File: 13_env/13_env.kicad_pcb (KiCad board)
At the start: 2 copper layers, 30 x 100 mm, 51 parts, among them J1 gate in 1, J3 Eurorack, J5 env out 1, J6 End of Cycle Out, Q1 BC848, Q2 BC858, Q3 BC848, Q4 BC858, SW1 Manual Gate, SW2 Normal/Inverted, SW4 Gate/Loop, U1 TL074, U2 TL072

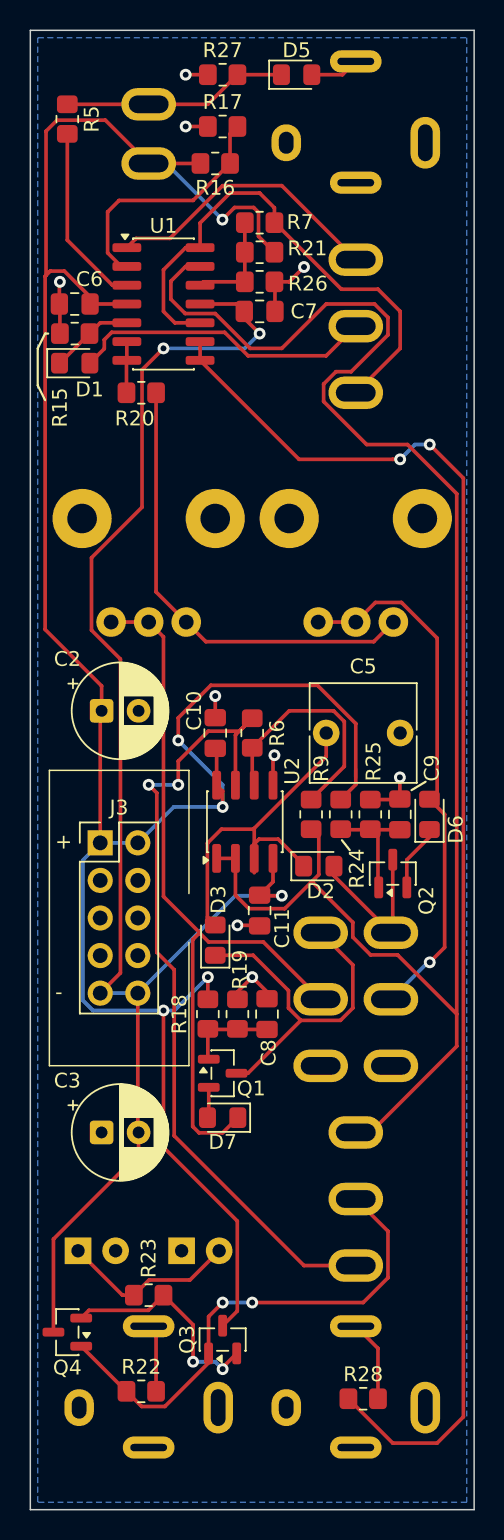
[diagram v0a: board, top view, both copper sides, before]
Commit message: added diodes
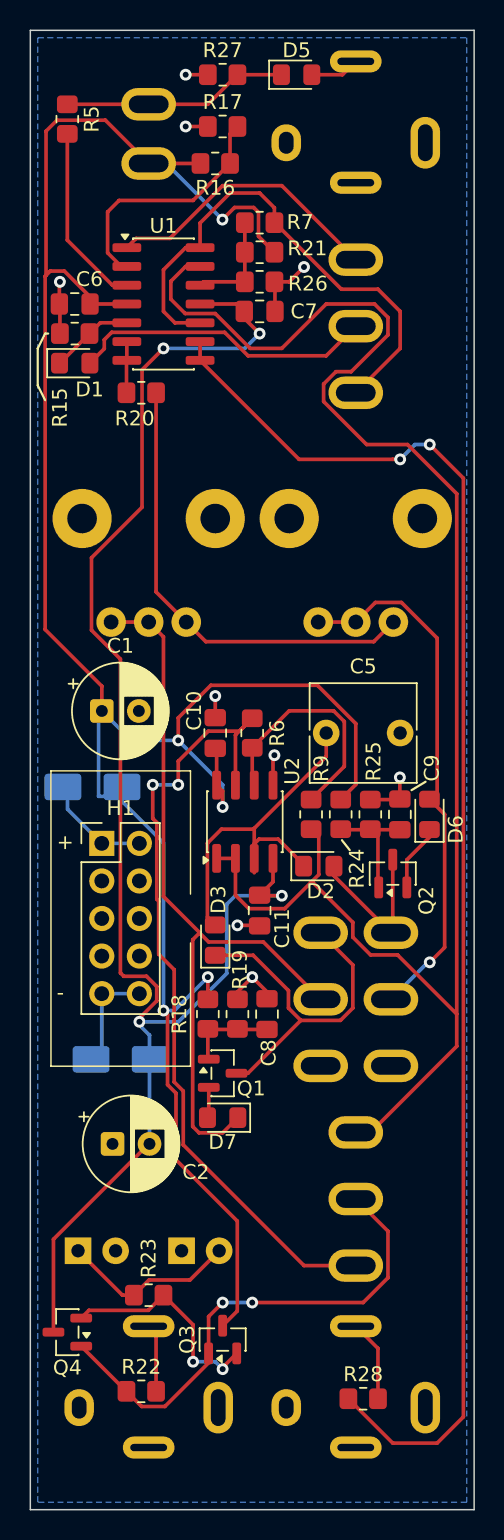
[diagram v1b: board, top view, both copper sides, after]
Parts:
- removed C3: 50uF, Capacitor_THT:CP_Radial_D6.3mm_P2.50mm
- removed J3: Eurorack, cynthia:Eurorack Header
- added C1: 22uF, Capacitor_THT:CP_Radial_D6.3mm_P2.50mm, F.Cu at (-0.17, 50.5)
- added D11: SS14, Diode_SMD:D_SMA, B.Cu at (1.10, 74.1)
- added D12: SS14, Diode_SMD:D_SMA, B.Cu at (-0.80, 55.6)
- added H1: Eurorack 10 pin header, cynthia:Eurorack Header, F.Cu at (-0.17, 59.5)
- C2: value 50uF -> 22uF
- moved C2 29.3 mm to (0.56, 79.8)
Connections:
- C2 pad 1: +12V -> GND
- C2 pad 2: GND -> -12V
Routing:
- net Net-(D11-K): track 0.00 -> 7.28 mm
- net +12V: track 168.9 -> 161.7 mm
- net Net-(D12-A): track 0.00 -> 6.68 mm
- net -12V: track 103.7 -> 107.1 mm, vias 3 -> 4

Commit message: updated 13 pcb
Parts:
- C1, C2, H1, Q1, Q2, Q3, Q4, U1, U2: moved to B.Cu
- C10, C11, C6, C7, C8, C9: footprint Capacitor_SMD:C_0805_2012Metric_Pad1.18x1.45mm_HandSolder -> cynthia:C SMD 0805; moved to B.Cu
- D1, D2, D3, D5, D6, D7: footprint Diode_SMD:D_0805_2012Metric_Pad1.15x1.40mm_HandSolder -> Diode_SMD:D_SOD-323_HandSoldering; moved to B.Cu
- D4, D8, J1, J5, J6, RV2, RV3, SW1, SW2, SW3, SW4: moved to F.Cu
- R15, R16, R17, R18, R19, R20, R21, R22, R23, R24, R25, R26, R27, R28, R5, R6, R7, R9: footprint Resistor_SMD:R_0805_2012Metric_Pad1.20x1.40mm_HandSolder -> cynthia:R SMD 0805; moved to B.Cu
- moved R28 85.0 mm to (17.0, 12.0), turned to 180 degrees
- moved J6 85.0 mm to (17.0, 12.0), turned to 0 degrees
- moved D11 36.7 mm to (-2.00, 37.5), turned to -90 degrees
- moved C2 32.7 mm to (4.18, 47.3), turned to 180 degrees
- moved R24 30.3 mm to (-2.50, 81.5), turned to -90 degrees
- moved R25 30.0 mm to (0.00, 81.5), turned to 90 degrees
- moved C9 29.7 mm to (2.50, 81.5), turned to -90 degrees
- moved D12 27.8 mm to (22.0, 39.8), turned to 90 degrees
- moved R5 27.4 mm to (23.0, 20.5), turned to 90 degrees
- moved D6 26.4 mm to (3.67, 76.5), turned to -90 degrees
- moved D8 26.0 mm to (21.5, 98.5), turned to 180 degrees
- moved H1 24.9 mm to (15.2, 39.9), turned to 90 degrees
- moved Q2 24.2 mm to (0.50, 76.5), turned to 0 degrees
- moved SW1 20.9 mm to (17.0, 27.0), turned to 0 degrees
- moved RV2 19.4 mm to (3.00, 51.0), turned to 0 degrees
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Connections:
- R20 pad 1: Net-(U1B--) -> Net-(U1D--)
- R21 pad 1: Net-(U1D-+) -> Net-(U1B-+)
- R26 pad 2: Net-(U1D-+) -> Net-(U1B-+)
- R7 pad 1: Net-(U1D-+) -> Net-(U1B-+)
- U1 pad 12: Net-(U1D-+) -> Net-(D1-K)
- U1 pad 13: Net-(SW2-A) -> Net-(U1D--)
- U1 pad 14: Net-(SW4-A) -> Net-(U1D--)
- U1 pad 5: Net-(D1-K) -> Net-(U1B-+)
- U1 pad 6: Net-(U1B--) -> Net-(SW2-A)
- U1 pad 7: Net-(U1B--) -> Net-(SW4-A)
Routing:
- net Net-(U1C--): track 96.4 -> 21.2 mm, vias 2 -> 0
- net Net-(D5-K): track 15.3 -> 57.5 mm
- net Net-(SW2-C): track 55.1 -> 21.9 mm, vias 2 -> 0
- net Net-(SW2-A): track 115.4 -> 88.8 mm, vias 0 -> 4
- net +12V: track 161.7 -> 140.4 mm, vias 5 -> 4
- net Net-(D1-A): track 20.7 -> 4.21 mm
- net Net-(U1B-+): track 0.00 -> 16.0 mm
- net Net-(Q3-B): track 34.1 -> 49.5 mm, vias 2 -> 0
- net Net-(D4-A): track 12.0 -> 27.1 mm
- net Net-(U1D--): track 0.00 -> 14.2 mm, vias 0 -> 2
- net Net-(R20-Pad2): track 31.4 -> 45.6 mm
- net -12V: track 107.1 -> 119.8 mm, vias 4 -> 3
- net Net-(D3-K): track 24.0 -> 12.3 mm
- net Net-(D2-K): track 26.0 -> 17.0 mm
- net Net-(U2B--): track 16.9 -> 8.05 mm
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- added copper zone on F.Cu, net GND
- removed copper zone on B.Cu, net GND
